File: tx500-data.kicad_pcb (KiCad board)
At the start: 2 copper layers, 79 x 50 mm, 42 parts, among them J1 USB_B, J2 CAT, J3 REM/DATA, J4 USB_A, U1 TUSB2036, U2 FT232RL, U3 HS-100B, U4 TPS76333, Y1 6MHz

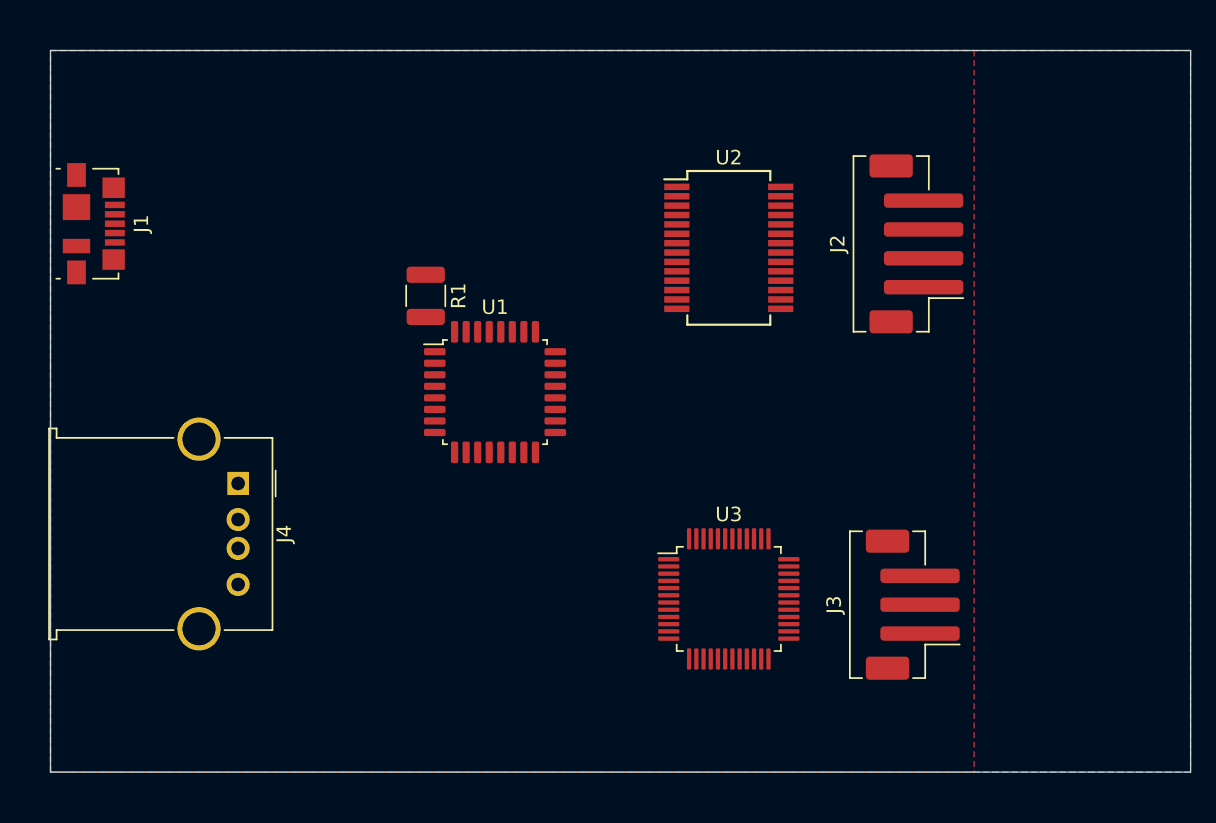
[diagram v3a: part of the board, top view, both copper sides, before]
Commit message: Add ID markings on schema and pcb
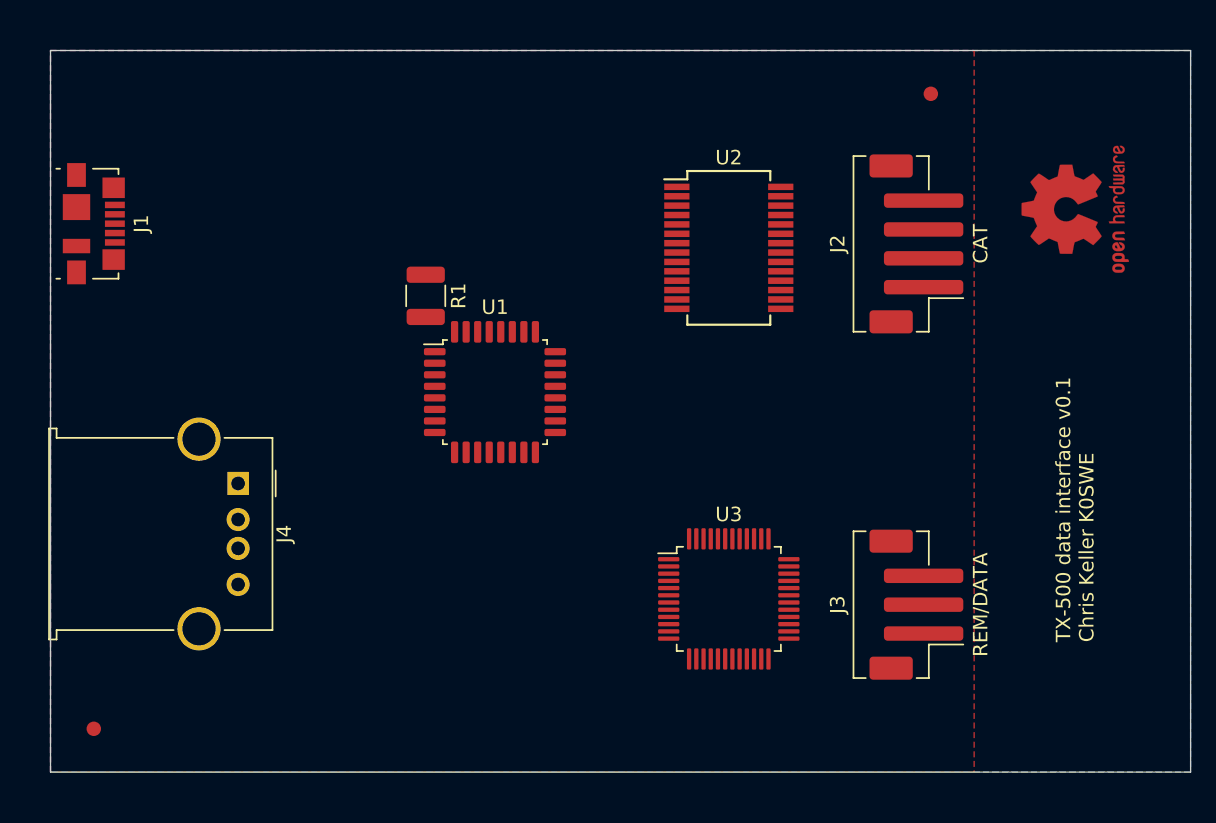
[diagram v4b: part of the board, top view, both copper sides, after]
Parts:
- added FID1: Fiducial, Fiducial:Fiducial_1mm_Mask2mm, F.Cu at (117.0, 113.0)
- added FID2: Fiducial, Fiducial:Fiducial_1mm_Mask2mm, F.Cu at (175.0, 69.0)
- added REF**: OSHW-Logo2_9.8x8mm_Copper, Symbol:OSHW-Logo2_9.8x8mm_Copper, F.Cu at (185.0, 77.0)
- moved J3 0.25 mm to (174.0, 104.4)
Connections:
- net /Upstream USB/US_33 renamed +3V3
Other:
- board text added: "TX-500 data interface v0.1 Chris Keller K0SWE"

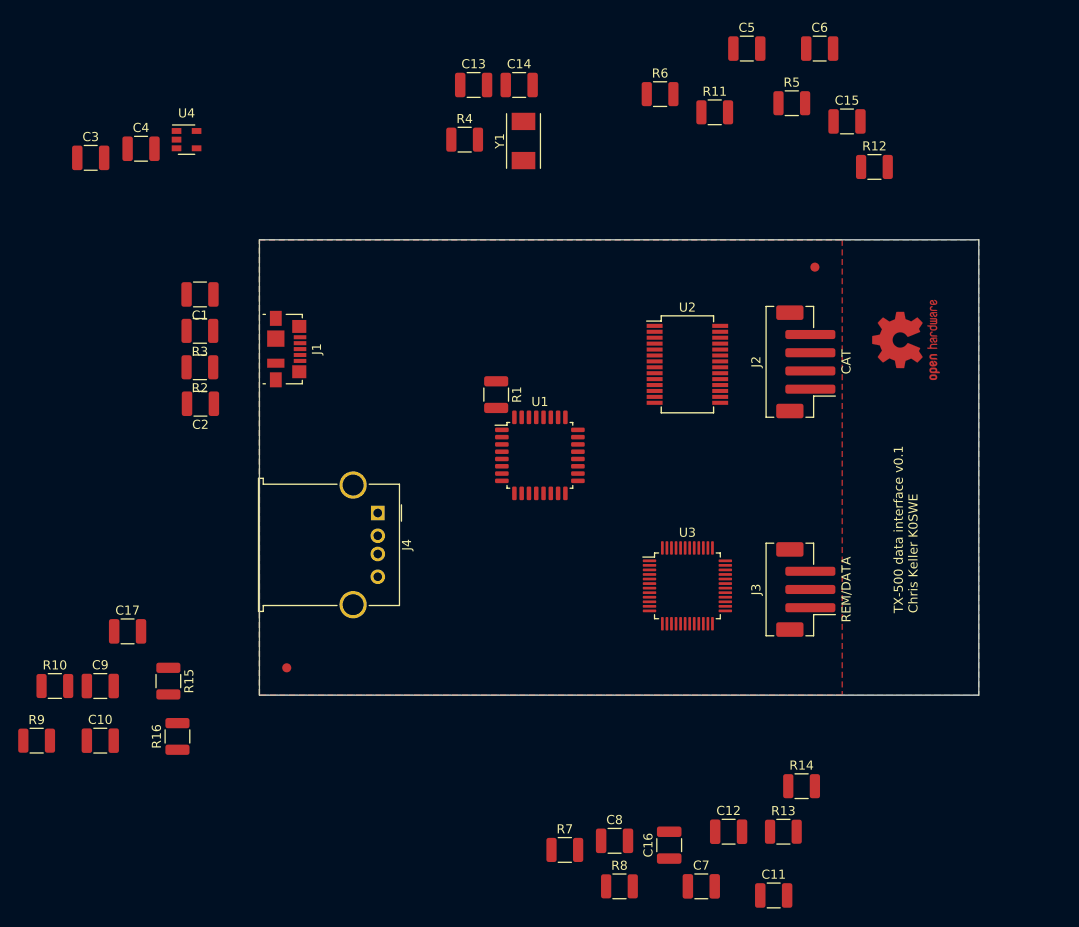
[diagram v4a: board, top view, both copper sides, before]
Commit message: First pass at routing PCB
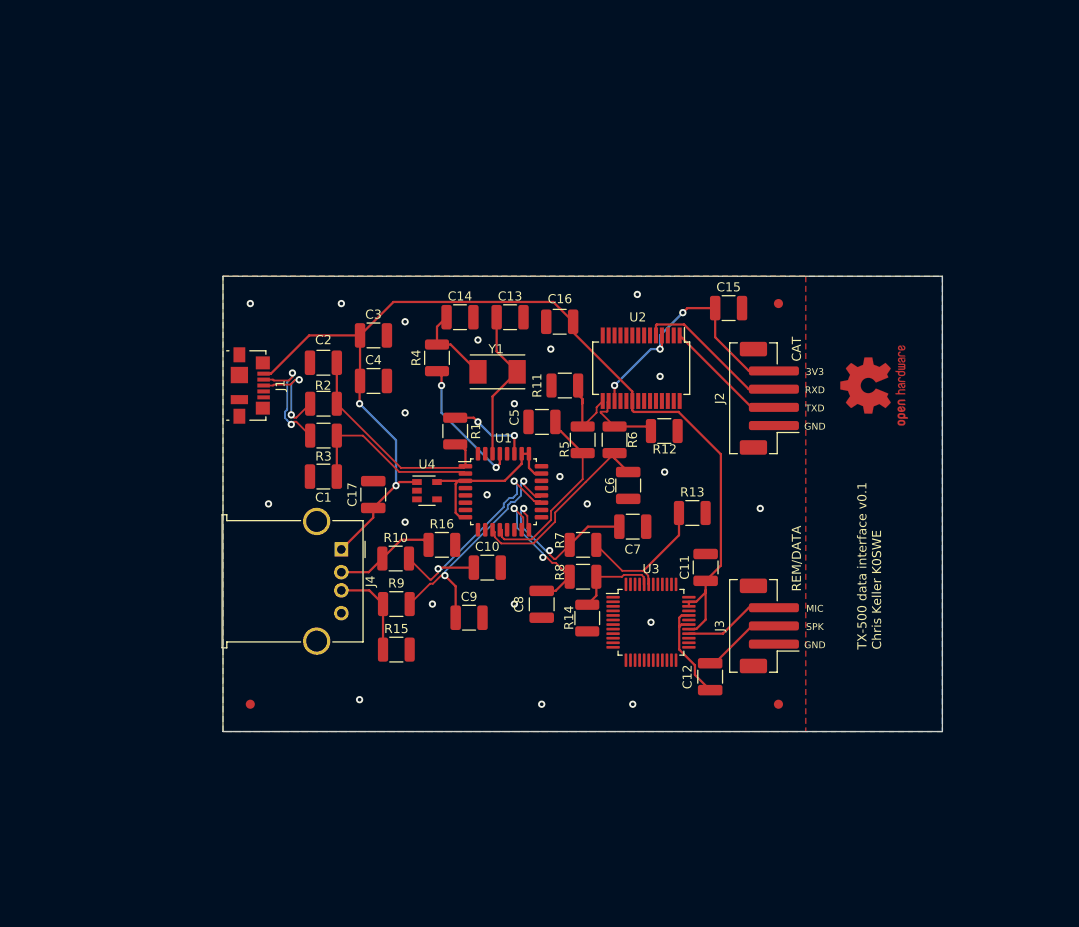
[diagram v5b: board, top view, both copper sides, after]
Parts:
- removed REF**: OSHW-Logo2_9.8x8mm_Copper, Symbol:OSHW-Logo2_9.8x8mm_Copper
- added FID3: Fiducial, Fiducial:Fiducial_1mm_Mask2mm, F.Cu at (171.0, 117.0)
- added LOGO1: Logo_Open_Hardware_Large, Symbol:OSHW-Logo2_9.8x8mm_Copper, F.Cu at (181.5, 82.0)
- moved C16 58.7 mm to (147.0, 75.0), turned to 180 degrees
- moved C6 52.4 mm to (154.5, 93.0), turned to 270 degrees
- moved C5 46.8 mm to (145.0, 86.0), turned to 180 degrees
- moved U4 46.7 mm to (132.4, 93.5)
- moved C10 46.6 mm to (139.0, 102.0)
- moved R5 43.5 mm to (149.5, 88.0), turned to 270 degrees
- moved R9 42.3 mm to (129.0, 106.0)
- moved C9 41.2 mm to (137.0, 107.5)
- moved C7 40.2 mm to (155.0, 97.5)
- moved R10 40.0 mm to (129.0, 101.0)
- moved R6 38.3 mm to (153.0, 88.0), turned to 270 degrees
- moved R12 37.1 mm to (158.5, 87.0)
- moved C11 36.8 mm to (163.0, 102.0), turned to 90 degrees
- moved C3 36.7 mm to (126.5, 76.5)
- moved R13 36.4 mm to (161.5, 96.0)
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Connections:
- net /Audio Interface/USB_DM renamed /Audio Interface/D-
- net /Audio Interface/USB_DP renamed /Audio Interface/D+
- net /CAT Conrol/USB_DM renamed /CAT Conrol/D-
- net /CAT Conrol/USB_DP renamed /CAT Conrol/D+
- net /Clock/XTAL1 renamed /XTAL1
- net /Clock/XTAL2 renamed /XTAL2
- net /Downstream USB/USB_DM renamed /Downstream USB/D-
- net /Downstream USB/USB_DP renamed /Downstream USB/D+
- net /Upstream USB/USB_DM renamed /D0-
- net /Upstream USB/USB_DP renamed /D0+
- net Net-(C10-Pad1) renamed /D3-
- net Net-(C12-Pad2) renamed /Audio Interface/LineOut
- net Net-(C5-Pad1) renamed /D1+
- net Net-(C6-Pad1) renamed /D1-
- net Net-(C7-Pad1) renamed /D2+
- net Net-(C8-Pad1) renamed /D2-
- net Net-(C9-Pad1) renamed /D3+
- net Net-(J1-Pad2) renamed /Upstream USB/DR-
- net Net-(J1-Pad3) renamed /Upstream USB/DR+
- C12 pad 1: Net-(C12-Pad1) -> /Audio Interface/SPK
- C15 pad 1: Net-(C15-Pad1) -> /CAT Conrol/3V3
- J1 pad 5: Net-(J1-Pad5) -> (no net)
- J2 pad 2: Net-(J2-Pad2) -> /CAT Conrol/TXD
- J2 pad 3: Net-(C15-Pad1) -> /CAT Conrol/RXD
- J2 pad 4: Net-(J2-Pad4) -> /CAT Conrol/3V3
- J3 pad 1: Net-(C12-Pad1) -> GNDREF
- J3 pad 2: Net-(J3-Pad2) -> /Audio Interface/SPK
- J3 pad 3: GNDREF -> /Audio Interface/MIC
- U1 pad 10: Net-(U1-Pad10) -> (no net)
- U1 pad 13: Net-(U1-Pad13) -> (no net)
- U1 pad 14: Net-(U1-Pad14) -> (no net)
- U1 pad 17: Net-(U1-Pad17) -> (no net)
- U1 pad 18: Net-(U1-Pad18) -> (no net)
- U1 pad 21: Net-(U1-Pad21) -> (no net)
- U1 pad 23: Net-(U1-Pad23) -> /3V3
- U1 pad 25: +3V3 -> /3V3
- U1 pad 26: Net-(U1-Pad23) -> /3V3
- U1 pad 3: +3V3 -> /3V3
- U1 pad 32: Net-(U1-Pad32) -> (no net)
- U1 pad 4: Net-(U1-Pad4) -> (no net)
- U1 pad 5: Net-(U1-Pad5) -> (no net)
- U1 pad 8: Net-(U1-Pad23) -> /3V3
- U1 pad 9: Net-(U1-Pad9) -> (no net)
- U2 pad 1: Net-(J2-Pad4) -> /CAT Conrol/TXD
- U2 pad 10: Net-(U2-Pad10) -> (no net)
- U2 pad 11: Net-(U2-Pad11) -> (no net)
- U2 pad 12: Net-(U2-Pad12) -> (no net)
- U2 pad 13: Net-(U2-Pad13) -> (no net)
- U2 pad 14: Net-(U2-Pad14) -> (no net)
- U2 pad 17: Net-(C15-Pad1) -> /CAT Conrol/3V3
- U2 pad 19: Net-(U2-Pad19) -> (no net)
- U2 pad 2: Net-(U2-Pad2) -> (no net)
- U2 pad 22: Net-(U2-Pad22) -> (no net)
- U2 pad 23: Net-(U2-Pad23) -> (no net)
- U2 pad 27: Net-(U2-Pad27) -> (no net)
- U2 pad 28: Net-(U2-Pad28) -> (no net)
- U2 pad 3: Net-(U2-Pad3) -> (no net)
- U2 pad 4: Net-(C15-Pad1) -> /CAT Conrol/3V3
- U2 pad 5: Net-(J2-Pad2) -> /CAT Conrol/RXD
- U2 pad 6: Net-(U2-Pad6) -> (no net)
- U2 pad 9: Net-(U2-Pad9) -> (no net)
- U3 pad 1: Net-(U3-Pad1) -> (no net)
- U3 pad 11: Net-(U3-Pad11) -> (no net)
- U3 pad 13: Net-(U3-Pad13) -> (no net)
- U3 pad 14: Net-(U3-Pad14) -> (no net)
- U3 pad 15: Net-(U3-Pad15) -> (no net)
- U3 pad 16: Net-(U3-Pad16) -> (no net)
- U3 pad 17: Net-(U3-Pad17) -> (no net)
- U3 pad 18: Net-(U3-Pad18) -> (no net)
- U3 pad 19: Net-(U3-Pad19) -> (no net)
- U3 pad 2: Net-(U3-Pad2) -> (no net)
- U3 pad 21: Net-(U3-Pad21) -> (no net)
- U3 pad 22: Net-(U3-Pad22) -> (no net)
- U3 pad 23: Net-(U3-Pad23) -> (no net)
- U3 pad 24: Net-(U3-Pad24) -> (no net)
- U3 pad 26: Net-(U3-Pad26) -> (no net)
- U3 pad 27: Net-(U3-Pad27) -> (no net)
- U3 pad 28: Net-(J3-Pad2) -> /Audio Interface/MIC
- U3 pad 3: Net-(U3-Pad3) -> (no net)
- U3 pad 31: Net-(U3-Pad31) -> (no net)
- U3 pad 37: Net-(U3-Pad37) -> (no net)
- U3 pad 38: Net-(U3-Pad38) -> (no net)
- U3 pad 39: Net-(U3-Pad39) -> (no net)
- U3 pad 4: Net-(U3-Pad4) -> (no net)
- U3 pad 41: Net-(U3-Pad41) -> (no net)
- U3 pad 42: Net-(U3-Pad42) -> (no net)
- U3 pad 45: Net-(U3-Pad45) -> (no net)
- U3 pad 46: Net-(U3-Pad46) -> (no net)
- U3 pad 47: Net-(U3-Pad47) -> (no net)
- U3 pad 48: Net-(U3-Pad48) -> (no net)
- U3 pad 5: Net-(U3-Pad5) -> (no net)
- U3 pad 7: Net-(U3-Pad7) -> (no net)
- U3 pad 9: Net-(U3-Pad9) -> (no net)
- U4 pad 3: Net-(U4-Pad3) -> (no net)
- U4 pad 4: Net-(U4-Pad4) -> (no net)
- U4 pad 5: +3V3 -> /3V3
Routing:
- net VBUS: track 0.00 -> 116.6 mm, vias 0 -> 2
- net /CAT Conrol/3V3: track 0.00 -> 29.9 mm, vias 0 -> 3
- net /D3+: track 0.00 -> 27.4 mm, vias 0 -> 2
- net /D3-: track 0.00 -> 26.7 mm, vias 0 -> 2
- net /D0+: track 0.00 -> 24.3 mm
- net /D1-: track 0.00 -> 22.3 mm
- net /3V3: track 0.00 -> 20.9 mm
- net /D1+: track 0.00 -> 20.8 mm
- net /D0-: track 0.00 -> 20.4 mm
- net /D2+: track 0.00 -> 18.6 mm, vias 0 -> 2
- net /D2-: track 0.00 -> 17.1 mm, vias 0 -> 2
- net /CAT Conrol/RXD: track 0.00 -> 17.0 mm
- net /XTAL1: track 0.00 -> 17.0 mm
- net /Audio Interface/D+: track 0.00 -> 16.0 mm
- net /XTAL2: track 0.00 -> 14.9 mm, vias 0 -> 2
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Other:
- board text added: "3V3"
- board text added: "GND"
- board text added: "MIC"
- board text added: "RXD"
- board text added: "SPK"
- board text added: "TXD"

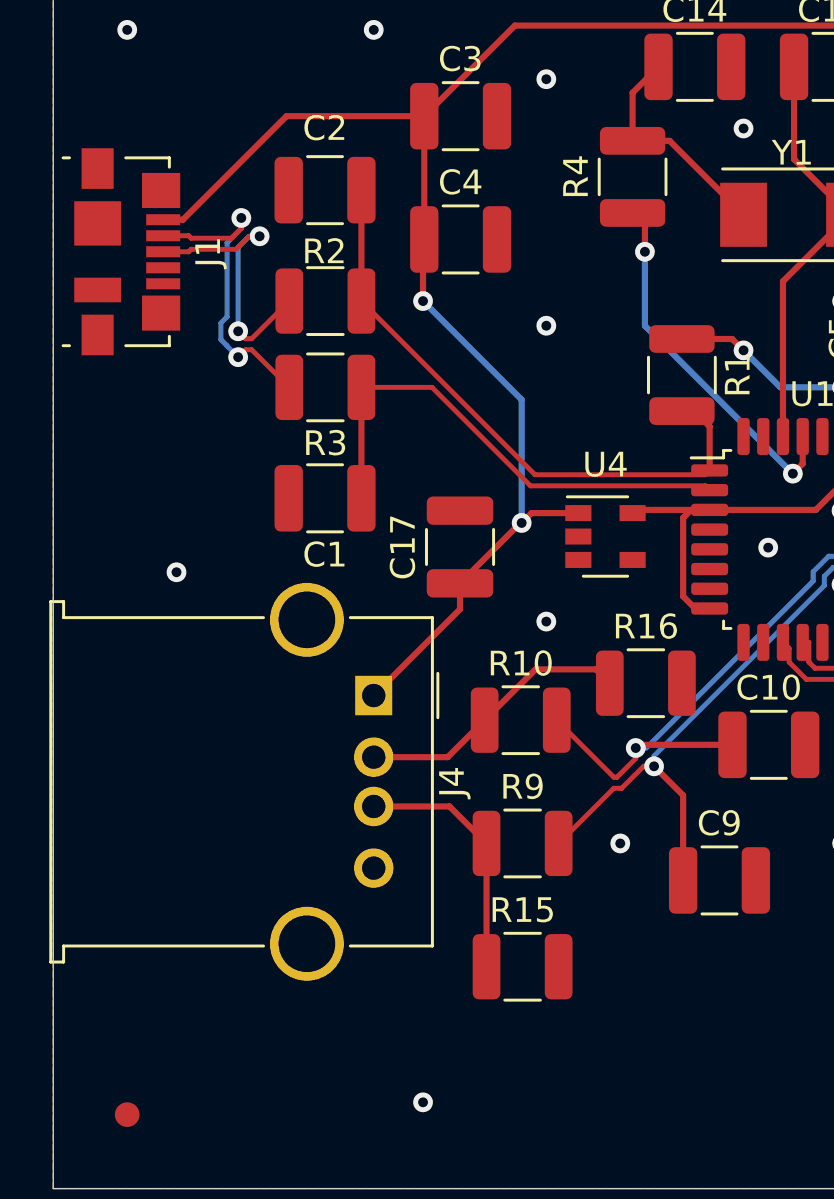
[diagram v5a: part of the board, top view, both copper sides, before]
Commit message: Replace USB-A port with SMD
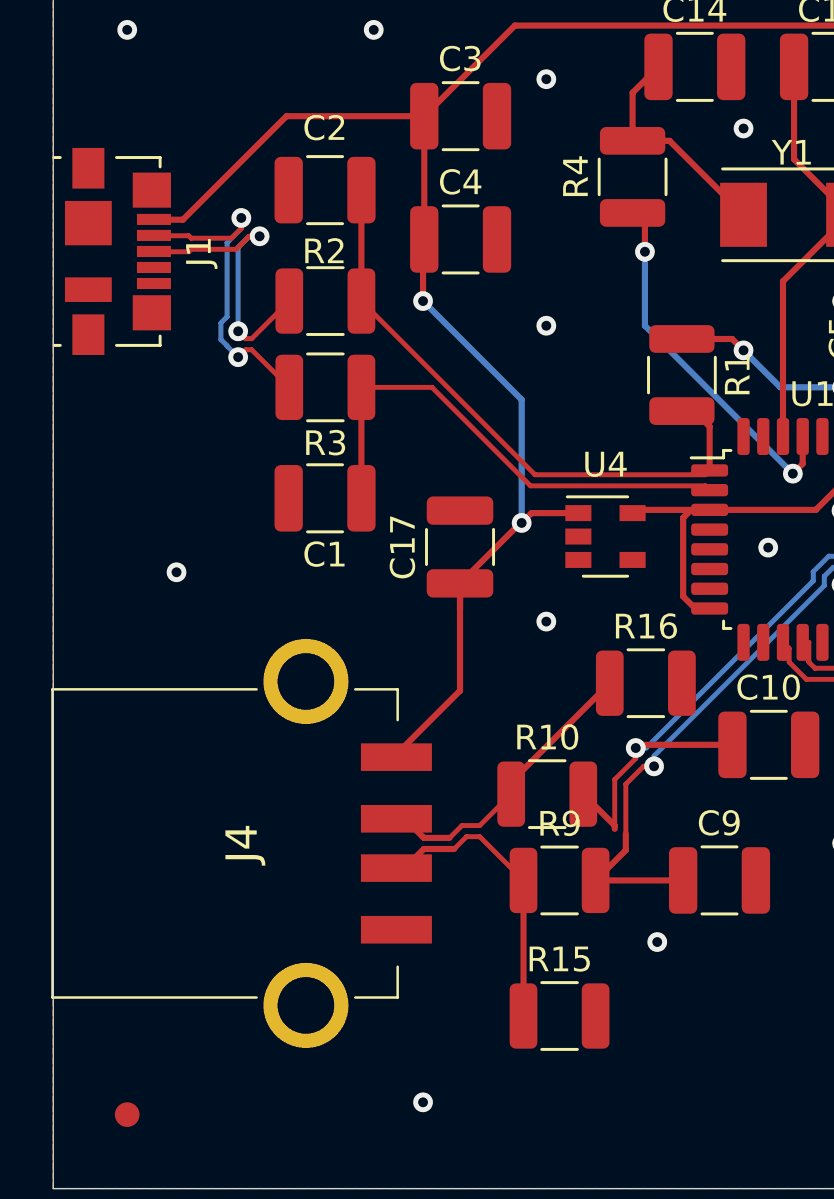
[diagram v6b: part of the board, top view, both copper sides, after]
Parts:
- J4: footprint Connector_USB:USB_A_Molex_67643_Horizontal -> Wurth-USBA:62900416021
- moved J4 8.03 mm to (117.7, 106.0)
- moved R10 3.19 mm to (130.0, 104.0)
- moved R15 2.50 mm to (130.5, 113.0)
- moved R9 2.12 mm to (130.5, 107.5)
- moved J1 0.38 mm to (112.6, 82.0)
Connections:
- J4 pad 5: Net-(J4-Pad5) -> (no net)
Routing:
- net VBUS: track 116.6 -> 119.1 mm, vias 2 -> 3
- net /Downstream USB/D+: track 10.2 -> 11.1 mm
- net /D3+: track 27.4 -> 26.6 mm
- net /D3-: track 26.7 -> 27.3 mm
- net GNDREF: vias 22 -> 21
